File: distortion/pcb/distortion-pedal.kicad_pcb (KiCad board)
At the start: 4 copper layers, 36 x 93 mm, 54 parts, among them J1 AudioJack2_Ground, J2 AudioJack2_Ground, J3 USB4125-GF-A-0190, SW1 SW_DPDT_x2, U1 LMR62014XMF-NOPB, U2 TL081H, U3 TL081H, U4 TL081H, U5 TLV767

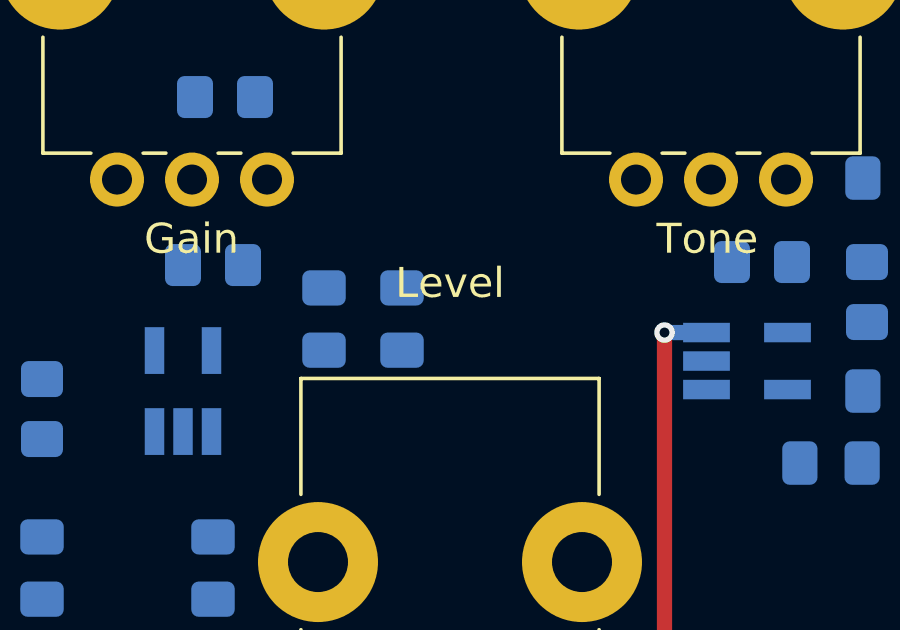
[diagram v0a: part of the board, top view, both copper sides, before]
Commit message: add circuit dimensioning
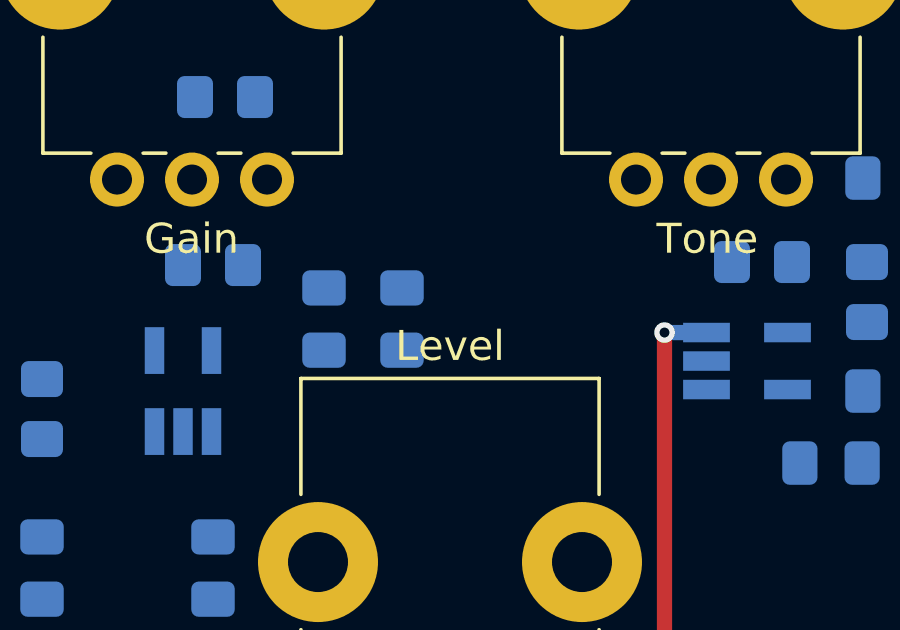
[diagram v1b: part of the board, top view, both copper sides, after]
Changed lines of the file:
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@@
     (effects (font (size 1 1) (thickness 0.15)))
   )
-  (gr_text "Level" (at 198 58.7) (layer "F.SilkS")
+  (gr_text "Level" (at 198 60.8) (layer "F.SilkS")
     (effects (font (size 1 1) (thickness 0.15)))
   )
@@
     (connect_pads yes (clearance 0))
     (min_thickness 0.254)
-    (keepout (tracks not_allowed) (vias not_allowed) (pads not_allowed ) (copperpour not_allowed) (footprints allowed))
-    (fill (thermal_gap 0.254) (thermal_bridge_width 0.508) (smoothing fillet) (radius 0.5))
+    (keepout (tracks not_allowed) (vias not_allowed) (pads not_allowed) (copperpour not_allowed) (footprints allowed))
+    (fill (thermal_gap 0.254) (thermal_bridge_width 0.508))
     (polygon
       (pts

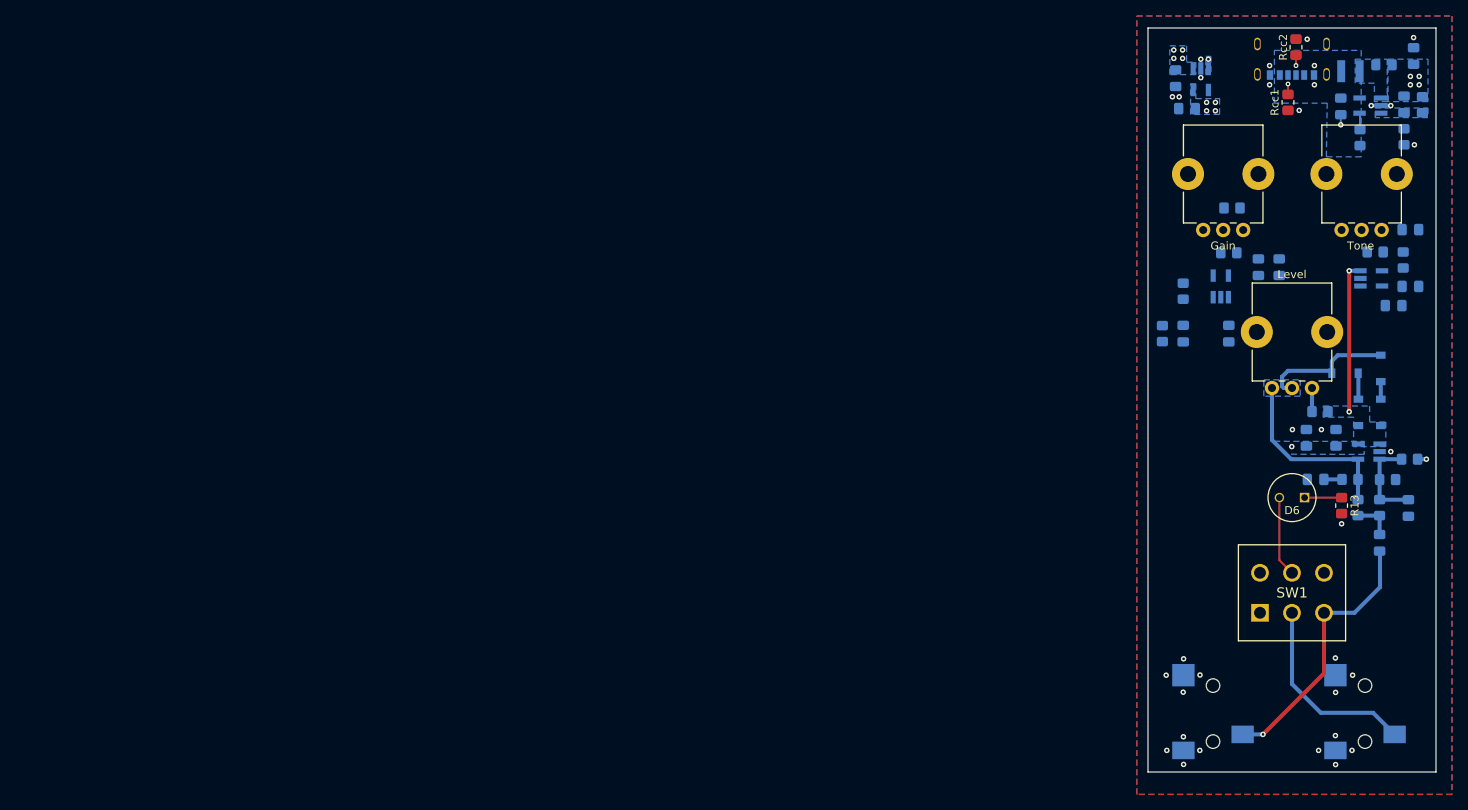
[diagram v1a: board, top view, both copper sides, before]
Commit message: rework distortion circuit and simulations
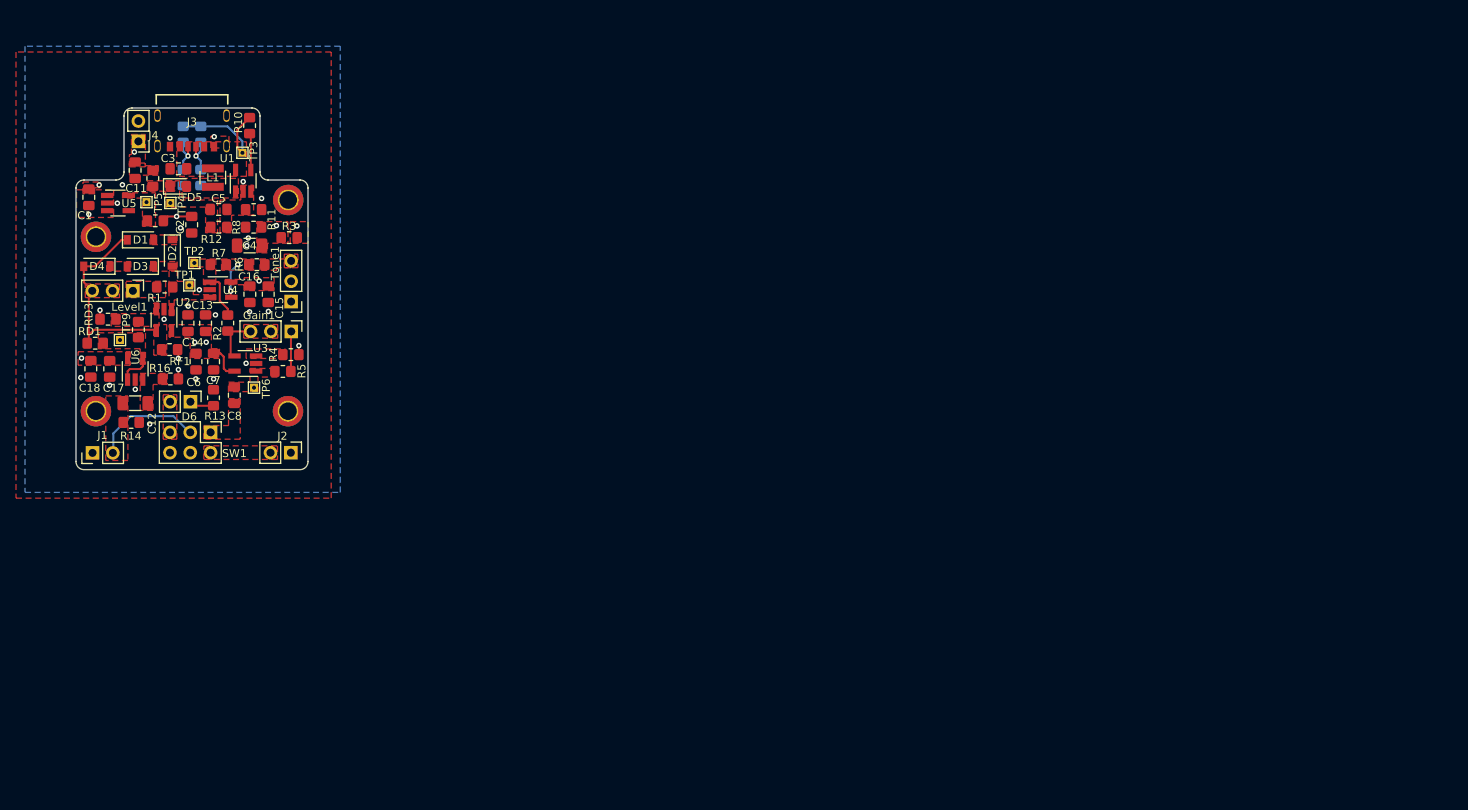
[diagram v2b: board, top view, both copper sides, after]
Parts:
- removed C10, C9, CF1, CF2: C, Capacitor_SMD:C_0805_2012Metric_Pad1.18x1.45mm_HandSolder
- removed R9: R, Resistor_SMD:R_0805_2012Metric_Pad1.20x1.40mm_HandSolder
- added C12: 22uF, Capacitor_SMD:C_1206_3216Metric_Pad1.33x1.80mm_HandSolder, F.Cu at (53.4, 76.9)
- added C17: 100nF, Capacitor_SMD:C_0805_2012Metric_Pad1.18x1.45mm_HandSolder, F.Cu at (50.2, 72.6)
- added C18: 10uF, Capacitor_SMD:C_0805_2012Metric_Pad1.18x1.45mm_HandSolder, F.Cu at (47.9, 72.6)
- added H1: MountingHole_Pad, MountingHole:MountingHole_2.2mm_M2_DIN965_Pad_TopBottom, F.Cu at (48.5, 56.1)
- added H2: MountingHole_Pad, MountingHole:MountingHole_2.2mm_M2_DIN965_Pad_TopBottom, F.Cu at (72.5, 51.5)
- added H3: MountingHole_Pad, MountingHole:MountingHole_2.2mm_M2_DIN965_Pad_TopBottom, F.Cu at (48.5, 77.9)
- added H4: MountingHole_Pad, MountingHole:MountingHole_2.2mm_M2_DIN965_Pad_TopBottom, F.Cu at (72.5, 77.9)
- added J4: Barrel_Jack, Connector_PinHeader_2.54mm:PinHeader_1x02_P2.54mm_Vertical, F.Cu at (53.8, 44.2)
- added JP1: Jumper_2_Open, Resistor_SMD:R_0805_2012Metric_Pad1.20x1.40mm_HandSolder, F.Cu at (55.6, 48.8)
- added JP2: Jumper_2_Open, Resistor_SMD:R_0805_2012Metric_Pad1.20x1.40mm_HandSolder, F.Cu at (55.9, 54.1)
- added R14: 510k, Resistor_SMD:R_0805_2012Metric_Pad1.20x1.40mm_HandSolder, F.Cu at (52.9, 79.3)
- added R16: 510k, Resistor_SMD:R_0805_2012Metric_Pad1.20x1.40mm_HandSolder, F.Cu at (57.8, 73.9)
- added RD3: R, Resistor_SMD:R_0805_2012Metric_Pad1.20x1.40mm_HandSolder, F.Cu at (50.0, 66.4)
- added Rcc3: 5.1k, Resistor_SMD:R_0805_2012Metric_Pad1.20x1.40mm_HandSolder, B.Cu at (61.6, 43.3)
- added Rcc4: 5.1k, Resistor_SMD:R_0805_2012Metric_Pad1.20x1.40mm_HandSolder, B.Cu at (59.4, 43.3)
- added TP1: TestPoint, TestPoint:TestPoint_THTPad_1.0x1.0mm_Drill0.5mm, F.Cu at (60.2, 62.2)
- added TP2: TestPoint, TestPoint:TestPoint_THTPad_1.0x1.0mm_Drill0.5mm, F.Cu at (60.8, 59.4)
- added TP3: TestPoint, TestPoint:TestPoint_THTPad_1.0x1.0mm_Drill0.5mm, F.Cu at (66.8, 45.6)
- added TP4: TestPoint, TestPoint:TestPoint_THTPad_1.0x1.0mm_Drill0.5mm, F.Cu at (57.8, 51.9)
- added TP5: TestPoint, TestPoint:TestPoint_THTPad_1.0x1.0mm_Drill0.5mm, F.Cu at (54.8, 51.8)
- added TP6: TestPoint, TestPoint:TestPoint_THTPad_1.0x1.0mm_Drill0.5mm, F.Cu at (68.2, 75.0)
- added TP9: TestPoint, TestPoint:TestPoint_THTPad_1.0x1.0mm_Drill0.5mm, F.Cu at (51.5, 69.0)
- added U6: TL081H, Package_TO_SOT_SMD:SOT-23-5_HandSoldering, F.Cu at (53.4, 72.6)
- C1, C11, C13, C14, C15, C16, C2, C3, C5, C6, C7, C8, D1, D2, D3, D4, D5, J3, JPF1, L1, R1, R10, R11, R12, R2, R4, R5, R6, R7, RD1, RF1, U1, U2, U3, U4, U5: moved to F.Cu
- C4: value C -> 33uF; footprint Capacitor_SMD:C_0805_2012Metric_Pad1.18x1.45mm_HandSolder -> Capacitor_SMD:C_1206_3216Metric_Pad1.33x1.80mm_HandSolder; moved to F.Cu
- D6: footprint effect_pedal:FB_28C0236-0EW-10 -> Connector_PinHeader_2.54mm:PinHeader_1x02_P2.54mm_Vertical
- Gain1, Level1, Tone1: footprint Potentiometer_THT:Potentiometer_Bourns_PTV09A-1_Single_Vertical -> Connector_PinHeader_2.54mm:PinHeader_1x03_P2.54mm_Vertical
- J1, J2: footprint effect_pedal:CUI_SJ-3523-SMT-TR-V2 -> Connector_PinHeader_2.54mm:PinHeader_1x02_P2.54mm_Vertical; moved to F.Cu
- R3, R8: value R -> 10k; moved to F.Cu
- Rcc1, Rcc2: moved to B.Cu
- SW1: footprint effect_pedal:SF12011F020220RL050 -> Connector_PinHeader_2.54mm:PinHeader_2x03_P2.54mm_Vertical
- moved C11 160.4 mm to (53.4, 47.8), turned to -90 degrees
- moved RD1 159.2 mm to (48.4, 69.4), turned to 180 degrees
- moved JPF1 156.7 mm to (53.8, 67.7)
- moved D4 156.6 mm to (48.6, 59.8)
- moved D1 155.9 mm to (54.1, 56.5), turned to 0 degrees
- moved D3 153.3 mm to (54.0, 59.8), turned to 180 degrees
- moved D2 152.4 mm to (58.0, 58.1)
- moved U2 151.5 mm to (57.0, 66.5), turned to -90 degrees
- moved D5 151.5 mm to (58.8, 49.8), turned to 0 degrees
- moved R12 151.2 mm to (63.8, 54.9), turned to 180 degrees
- moved C5 148.8 mm to (63.8, 52.7), turned to 180 degrees
- moved RF1 148.4 mm to (57.7, 70.2), turned to 0 degrees
- moved R7 148.1 mm to (63.8, 59.6), turned to 180 degrees
- moved Level1 147.9 mm to (53.1, 62.9), turned to -90 degrees
- moved R8 147.4 mm to (68.2, 54.9), turned to 0 degrees
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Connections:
- net Net-(C9-Pad2) renamed effect_in
- C4 pad 1: Net-(C4-Pad1) -> +4V
- C5 pad 2: +9V -> Net-(C5-Pad2)
- D5 pad 1: +9V -> Net-(C5-Pad2)
- J1 pad 2: GND -> audio_in
- J2 pad 2: GND -> Net-(J2-Pad2)
- JPF1 pad 2: Net-(CF1-Pad1) -> Net-(JPF1-Pad2)
- R12 pad 2: +9V -> Net-(C5-Pad2)
- R3 pad 1: +8V -> +4V
- R3 pad 2: Net-(C4-Pad1) -> +8V
- R4 pad 1: Net-(C4-Pad1) -> Net-(R4-Pad1)
- R4 pad 2: GND -> +4V
- R8 pad 1: +8V -> GND
- R8 pad 2: Net-(CF1-Pad1) -> +4V
- RF1 pad 2: Net-(CF2-Pad1) -> +4V
- SW1 pad 2: Net-(J2-Pad3) -> Net-(J2-Pad2)
- Tone1 pad 1: Net-(C10-Pad1) -> +4V
- Tone1 pad 2: Net-(R6-Pad1) -> +4V
- U2 pad 3: Net-(CF1-Pad1) -> Net-(JPF1-Pad2)
- U3 pad 3: Net-(C4-Pad1) -> Net-(R4-Pad1)
- U5 pad 5: +8V -> Net-(U5-Pad5)
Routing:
- net Net-(J2-Pad3): track 24.3 -> 0.00 mm
- net audio_in: track 33.7 -> 13.7 mm, vias 1 -> 0
- net Net-(D2-Pad2): track 19.0 -> 0.00 mm, vias 2 -> 0
- net +5V: track 0.00 -> 14.9 mm
- net Net-(D1-Pad1): track 40.4 -> 26.7 mm
- net Net-(CF1-Pad1): track 11.4 -> 0.00 mm
- net Net-(D6-Pad2): track 10.1 -> 0.00 mm
- net +8V: track 1.10 -> 8.49 mm
- net Net-(Gain1-Pad2): track 0.00 -> 6.12 mm
- net effect_out: track 0.00 -> 5.78 mm
- net Net-(Gain1-Pad1): track 0.00 -> 4.67 mm
- net Net-(R6-Pad2): track 0.00 -> 4.43 mm, vias 0 -> 2
- net +4V: track 0.00 -> 4.26 mm, vias 0 -> 5
- net GND: track 3.71 -> 0.00 mm, vias 34 -> 23
- net Net-(J3-PadB5): track 1.40 -> 5.07 mm
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- added copper zone on F.Cu, net +4V
- added copper zone on In1.Cu, net +4V
- added copper zone on F.Cu, net +5V
- added copper zone on F.Cu, net +8V
- added copper zone on F.Cu, net +9V
- added copper zone on F.Cu, net Net-(C12-Pad2)
- added copper zone on F.Cu, net Net-(C5-Pad1)
- added copper zone on F.Cu, net Net-(C5-Pad2)
- added copper zone on F.Cu, net Net-(C8-Pad1)
- added copper zone on F.Cu, net Net-(D1-Pad1)
- added copper zone on F.Cu, net Net-(D1-Pad2)
- added copper zone on F.Cu, net Net-(D2-Pad2)
- added copper zone on F.Cu, net Net-(D3-Pad2)
- added copper zone on F.Cu, net Net-(D5-Pad2)
- added copper zone on F.Cu, net Net-(D6-Pad2)
- added copper zone on F.Cu, net Net-(Gain1-Pad2)
- added copper zone on F.Cu, net Net-(J2-Pad2)
- added copper zone on F.Cu, net Net-(JPF1-Pad2)
- added copper zone on F.Cu, net Net-(R1-Pad1)
- added copper zone on F.Cu, net Net-(R4-Pad1)
- added copper zone on F.Cu, net Net-(R6-Pad1)
- added copper zone on F.Cu, net Net-(R6-Pad2)
- added copper zone on F.Cu, net Net-(U5-Pad5)
- added copper zone on F.Cu, net audio_in
- added copper zone on F.Cu, net effect_in
- added copper zone on F.Cu, net effect_out
- added copper zone on F.Cu, net gain_out
- removed copper zone on B.Cu, net +5V
- removed copper zone on B.Cu, net +8V
- removed copper zone on B.Cu, net +9V
- removed copper zone on In1.Cu, net GND
- removed copper zone on B.Cu, net Net-(C5-Pad1)
- removed copper zone on B.Cu, net Net-(D1-Pad1)
- removed copper zone on B.Cu, net Net-(D2-Pad2)
- removed copper zone on B.Cu, net Net-(D5-Pad2)
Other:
- board size 36 x 93 mm -> 29 x 45.2 mm
- board text removed: "Gain"
- board text removed: "Level"
- board text removed: "Tone"
- board text removed: "audio in"
- board text removed: "audio out"

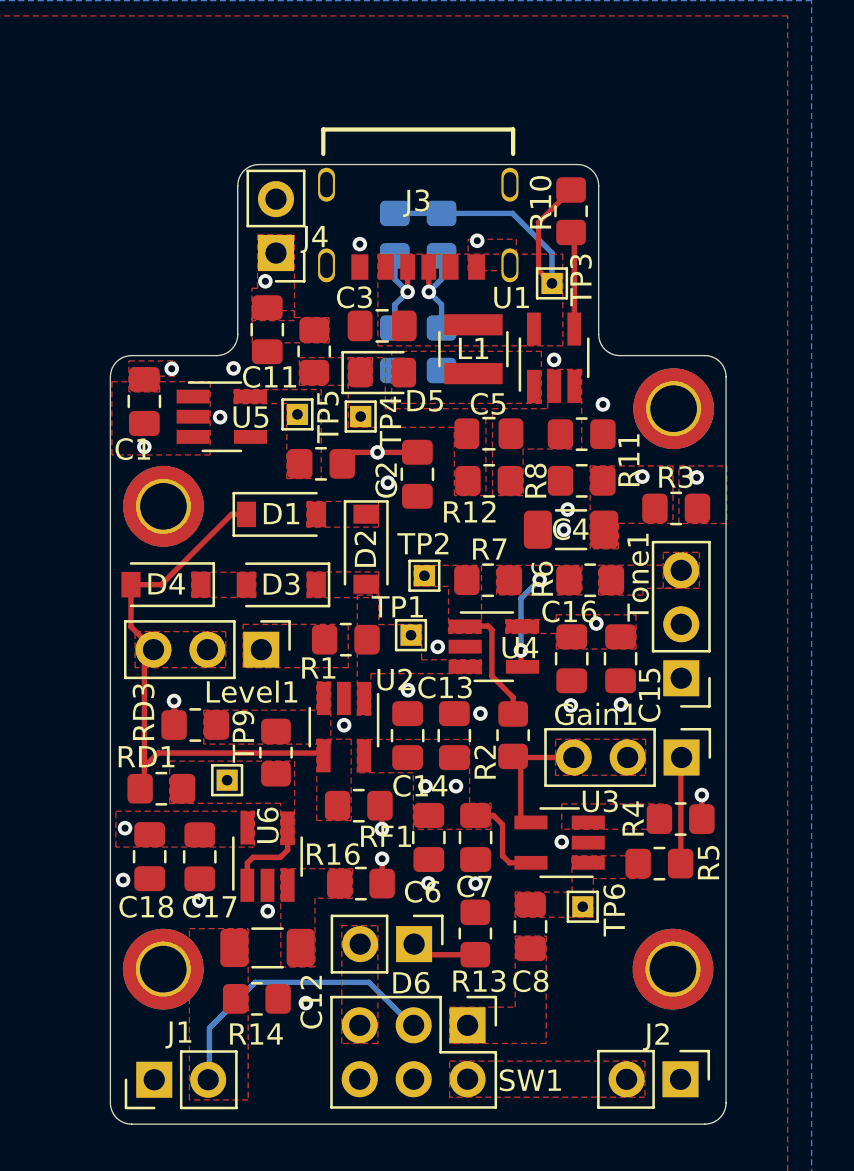
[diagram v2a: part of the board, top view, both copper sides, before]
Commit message: create gerber files, update BOM for REV2
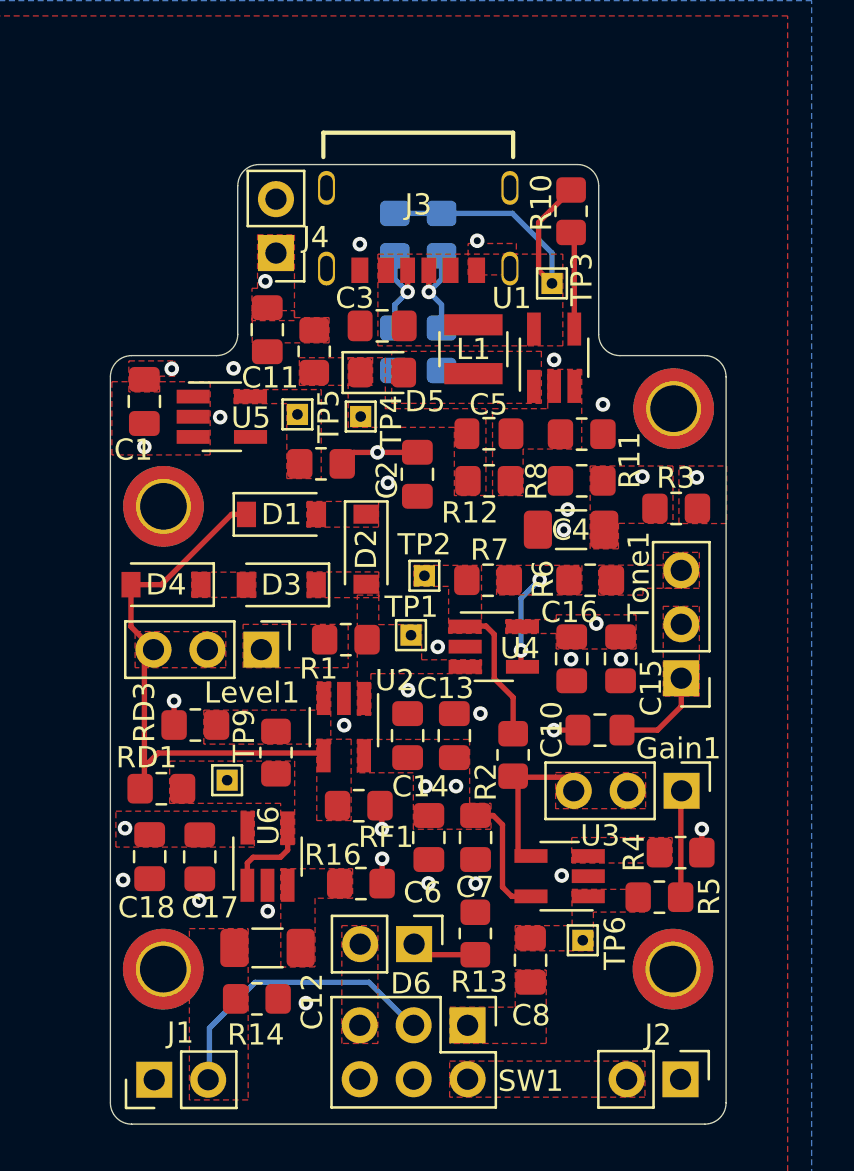
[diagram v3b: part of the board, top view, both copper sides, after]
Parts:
- added C10: 10uF, Capacitor_SMD:C_0805_2012Metric_Pad1.18x1.45mm_HandSolder, F.Cu at (69.1, 66.6)
- moved TP6 1.58 mm to (68.2, 76.5)
- moved C8 1.58 mm to (65.8, 77.5)
- moved R4 1.58 mm to (72.9, 72.4)
- moved R5 1.58 mm to (71.9, 74.5)
- moved U3 1.58 mm to (67.2, 73.5)
- moved Gain1 1.57 mm to (72.9, 69.5)
- moved R2 0.93 mm to (65.0, 67.8)
- moved J3 0.15 mm to (60.5, 41.9)
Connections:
- Tone1 pad 1: +4V -> Net-(Tone1-Pad1)
- Tone1 pad 2: +4V -> Net-(Tone1-Pad1)
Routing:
- net Net-(Tone1-Pad1): track 0.00 -> 4.58 mm
- net +8V: track 8.49 -> 10.0 mm
- net Net-(Gain1-Pad2): track 6.12 -> 7.38 mm
- net +4V: track 4.26 -> 5.40 mm, vias 5 -> 6
- net effect_out: track 5.78 -> 6.65 mm
- added copper zone on F.Cu, net Net-(Tone1-Pad1)
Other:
- board text added: "Fuzz/Distortion Pedal REV2"
